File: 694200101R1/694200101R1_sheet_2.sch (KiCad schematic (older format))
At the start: 48 parts

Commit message: Added 3D Models
Added 3D Models for all components
Added Keyboard DXF for reference
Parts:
- D168, D169, D170, D171, D172, D173, D174, D175, D176, D177, D178, D179, D180, D181, D182, D183, D184, D185, D186, D187, D188, D189, D190, D191, D192, D193, D194, D195, D196, D197, D198, D199, D200, D201, D202, D203, D204, D205, D206, D207, D208, D209, D210, D211, D212, D213, D214, D215: renamed from D?; footprint LED_19-337C/RSBHGHC-A88/4T -> RSBHGHC-A88:4T; symbol 694200101-rescue:19-337C_RSBHGHC-A88_4T-19-337C_RSBHGHC-A88_4T -> 19-337C_RSBHGHC-A88_4T:RGB_LED

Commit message: fixed file names, added additional source
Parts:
- removed D168, D169, D170, D171, D172, D173, D174, D175, D176, D177, D178, D179, D180, D181, D182, D183, D184, D185, D186, D187, D188, D189, D190, D191, D192, D193, D194, D195, D196, D197, D198, D199, D200, D201, D202, D203, D204, D205, D206, D207, D208, D209, D210, D211, D212, D213, D214, D215: 19-337C_RSBHGHC-A88_4T, RSBHGHC-A88:4T, symbol 19-337C_RSBHGHC-A88_4T:RGB_LED
- added C10, C11, C13, C18, C20, C21, C23, C8: CL10B474KA8NFNC, capacitor-lib:CAPC1608X90N, symbol capacitor-lib:CL10B474KA8NFNC
- added C12, C14, C17, C19, C22, C9: CL10B104KB8NNNL, capacitor-lib:Samsung-CL10-09_2006-0-IPC_C, symbol capacitor-lib:CL10B104KB8NNNL
- added C15, C16: TAJB226K016RNJ, capacitor-lib:CAPPC3528X210N, symbol capacitor-lib:TAJB226K016RNJ
- added D104, D105, D106, D107, D108, D109, D110, D111, D112, D113, D114, D115, D116, D117, D118, D119, D120, D121, D122, D123, D124, D125, D126, D127, D128, D129, D130, D131, D132, D133, D134, D135, D136, D137, D138, D139, D140, D141, D142, D143, D144, D145, D146, D147, D148, D149, D150, D151, D152, D153, D154, D155, D156, D157, D158, D159, D160, D161, D162, D163, D164, D165, D166, D167: 19-337C_RSBHGHC-A88_4T, RSBHGHC-A88:4T, symbol 19-337C_RSBHGHC-A88_4T:RGB_LED
- added R10, R12, R13, R9: RMCF0603FT100K, Resistor-Libs:RESC1508X55N, symbol Resistor-Lib:RMCF0603FT100K
- added R11, R14: RMCF2512FT20K0, Resistor-Libs:RESC6332X70N, symbol Resistor-Lib:RMCF2512FT20K0
- added U3: M24M02-DRMN6TP, STM:STMicroelectronics-SO8N-SO-A-0-2-IPC_C, symbol STM:M24M02-DRMN6TP
- added U4, U5: IS31FL3733B-QFLS4-TR, Lumissil:IS31FL3733B-QFLS4-TR, symbol Lumissil:IS31FL3733B-QFLS4-TR
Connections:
- net CS10_B: now also U5.26 (CS10)
- net CS11_B: now also U5.27 (CS11)
- net CS12_B: now also U5.28 (CS12)
- net CS1_B: now also U5.16 (CS1)
- net CS2_B: now also U5.17 (CS2)
- net CS3_B: now also U5.18 (CS3)
- net CS4_B: now also U5.19 (CS4)
- net CS5_B: now also U5.21 (CS5)
- net CS6_B: now also U5.22 (CS6)
- net CS7_B: now also U5.23 (CS7)
- net CS8_B: now also U5.24 (CS8)
- net CS9_B: now also U5.25 (CS9)
- net SW10_B: now also U5.13 (SW10)
- net SW11_B: now also U5.14 (SW11)
- net SW12_B: now also U5.15 (SW12)
- net SW1_B: now also U5.2 (SW1)
- net SW2_B: now also U5.3 (SW2)
- net SW3_B: now also U5.4 (SW3)
- net SW4_B: now also U5.6 (SW4)
- net SW5_B: now also U5.7 (SW5)
- net SW6_B: now also U5.8 (SW6)
- net SW7_B: now also U5.9 (SW7)
- net SW8_B: now also U5.10 (SW8)
- net SW9_B: now also U5.11 (SW9)
- new net: R11.1, U4.35 (RSET)
- new net: R9.1, U4.47 (IICRST)
- new net: R14.1, U5.35 (RSET)
- new net: U5.42 (SCL), U5.43 (ADDR1)
- new net: R12.1, U5.47 (IICRST)
- new net +3V3: C10.1, C11.1, C12.1, C13.1, C14.1, C15.1, C16.1, C17.1, C18.1, C19.1, C20.1, C21.1, C22.1, C23.1, C8.1, C9.1, R10.1, R13.1, U3.8 (VCC), U4.20 (PVCC), U4.29 (PVCC), U4.37 (AVCC), U4.38 (DVCC), U4.39 (VIO), U4.46 (SDB), U5.20 (PVCC), U5.29 (PVCC), U5.37 (AVCC), U5.38 (DVCC), U5.39 (VIO), U5.46 (SDB)
- new net CS10_A: D140.2, D140.4, D140.6, D141.2, D141.4, D141.6, D142.2, D142.4, D142.6, D143.2, D143.4, D143.6, U4.26 (CS10)
- new net CS11_A: D144.2, D144.4, D144.6, D145.2, D145.4, D145.6, D146.2, D146.4, D146.6, D147.2, D147.4, D147.6, U4.27 (CS11)
- new net CS12_A: D148.2, D148.4, D148.6, D149.2, D149.4, D149.6, D150.2, D150.4, D150.6, D151.2, D151.4, D151.6, U4.28 (CS12)
- new net CS13_A: D152.2, D152.4, D152.6, D153.2, D153.4, D153.6, D154.2, D154.4, D154.6, D155.2, D155.4, D155.6, U4.30 (CS13)
- new net CS13_B: U5.30 (CS13)
- new net CS14_A: D156.2, D156.4, D156.6, D157.2, D157.4, D157.6, D158.2, D158.4, D158.6, D159.2, D159.4, D159.6, U4.31 (CS14)
- new net CS14_B: U5.31 (CS14)
- new net CS15_A: D160.2, D160.4, D160.6, D161.2, D161.4, D161.6, D162.2, D162.4, D162.6, D163.2, D163.4, D163.6, U4.32 (CS15)
- new net CS15_B: U5.32 (CS15)
- new net CS16_A: D164.2, D164.4, D164.6, D165.2, D165.4, D165.6, D166.2, D166.4, D166.6, D167.2, D167.4, D167.6, U4.33 (CS16)
- new net CS16_B: U5.33 (CS16)
- new net CS1_A: D104.2, D104.4, D104.6, D105.2, D105.4, D105.6, D106.2, D106.4, D106.6, D107.2, D107.4, D107.6, U4.16 (CS1)
- new net CS2_A: D108.2, D108.4, D108.6, D109.2, D109.4, D109.6, D110.2, D110.4, D110.6, D111.2, D111.4, D111.6, U4.17 (CS2)
- new net CS3_A: D112.2, D112.4, D112.6, D113.2, D113.4, D113.6, D114.2, D114.4, D114.6, D115.2, D115.4, D115.6, U4.18 (CS3)
- new net CS4_A: D116.2, D116.4, D116.6, D117.2, D117.4, D117.6, D118.2, D118.4, D118.6, D119.2, D119.4, D119.6, U4.19 (CS4)
- new net CS5_A: D120.2, D120.4, D120.6, D121.2, D121.4, D121.6, D122.2, D122.4, D122.6, D123.2, D123.4, D123.6, U4.21 (CS5)
- new net CS6_A: D124.2, D124.4, D124.6, D125.2, D125.4, D125.6, D126.2, D126.4, D126.6, D127.2, D127.4, D127.6, U4.22 (CS6)
- new net CS7_A: D128.2, D128.4, D128.6, D129.2, D129.4, D129.6, D130.2, D130.4, D130.6, D131.2, D131.4, D131.6, U4.23 (CS7)
- new net CS8_A: D132.2, D132.4, D132.6, D133.2, D133.4, D133.6, D134.2, D134.4, D134.6, D135.2, D135.4, D135.6, U4.24 (CS8)
- new net CS9_A: D136.2, D136.4, D136.6, D137.2, D137.4, D137.6, D138.2, D138.4, D138.6, D139.2, D139.4, D139.6, U4.25 (CS9)
- new net GND: C10.2, C11.2, C12.2, C13.2, C14.2, C15.2, C16.2, C17.2, C18.2, C19.2, C20.2, C21.2, C22.2, C23.2, C8.2, C9.2, R10.2, R11.2, R12.2, R13.2, R14.2, R9.2, U3.1 (DU), U3.2 (DU), U3.3 (E2), U3.4 (VSS), U3.7 (~WC~), U4.12 (PGND), U4.34 (AGND), U4.43 (ADDR1), U4.44 (ADDR2), U4.48 (GND), U4.49 (HTAB), U4.5 (PGND), U5.12 (PGND), U5.34 (AGND), U5.44 (ADDR2), U5.48 (GND), U5.49 (HTAB), U5.5 (PGND)
- new net SW10_A: D104.1, D108.1, D112.1, D116.1, D120.1, D124.1, D128.1, D132.1, D136.1, D140.1, D144.1, D148.1, D152.1, D156.1, D160.1, D164.1, U4.13 (SW10)
- new net SW11_A: D104.3, D108.3, D112.3, D116.3, D120.3, D124.3, D128.3, D132.3, D136.3, D140.3, D144.3, D148.3, D152.3, D156.3, D160.3, D164.3, U4.14 (SW11)
- new net SW12_A: D104.5, D108.5, D112.5, D116.5, D120.5, D124.5, D128.5, D132.5, D136.5, D140.5, D144.5, D148.5, D152.5, D156.5, D160.5, D164.5, U4.15 (SW12)
- new net SW1_A: D107.1, D111.1, D115.1, D119.1, D123.1, D127.1, D131.1, D135.1, D139.1, D143.1, D147.1, D151.1, D155.1, D159.1, D163.1, D167.1, U4.2 (SW1)
- new net SW2_A: D107.3, D111.3, D115.3, D119.3, D123.3, D127.3, D131.3, D135.3, D139.3, D143.3, D147.3, D151.3, D155.3, D159.3, D163.3, D167.3, U4.3 (SW2)
- new net SW3_A: D107.5, D111.5, D115.5, D119.5, D123.5, D127.5, D131.5, D135.5, D139.5, D143.5, D147.5, D151.5, D155.5, D159.5, D163.5, D167.5, U4.4 (SW3)
- new net SW4_A: D106.1, D110.1, D114.1, D118.1, D122.1, D126.1, D130.1, D134.1, D138.1, D142.1, D146.1, D150.1, D154.1, D158.1, D162.1, D166.1, U4.6 (SW4)
- new net SW5_A: D106.3, D110.3, D114.3, D118.3, D122.3, D126.3, D130.3, D134.3, D138.3, D142.3, D146.3, D150.3, D154.3, D158.3, D162.3, D166.3, U4.7 (SW5)
- new net SW6_A: D106.5, D110.5, D114.5, D118.5, D122.5, D126.5, D130.5, D134.5, D138.5, D142.5, D146.5, D150.5, D154.5, D158.5, D162.5, D166.5, U4.8 (SW6)
- new net SW7_A: D105.1, D109.1, D113.1, D117.1, D121.1, D125.1, D129.1, D133.1, D137.1, D141.1, D145.1, D149.1, D153.1, D157.1, D161.1, D165.1, U4.9 (SW7)
- new net SW8_A: D105.3, D109.3, D113.3, D117.3, D121.3, D125.3, D129.3, D133.3, D137.3, D141.3, D145.3, D149.3, D153.3, D157.3, D161.3, D165.3, U4.10 (SW8)
- new net SW9_A: D105.5, D109.5, D113.5, D117.5, D121.5, D125.5, D129.5, D133.5, D137.5, D141.5, D145.5, D149.5, D153.5, D157.5, D161.5, D165.5, U4.11 (SW9)
- new net SYNC: U4.40 (SYNC), U5.40 (SYNC)
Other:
- note added: "LED_DRIVER_A\nP20"
- note added: "LED_DRIVER_A\nP29"
- note added: "LED_DRIVER_A\nP37/38"
- note added: "LED_DRIVER_A\nP39"
- note added: "LED_DRIVER_A\nPWR_FILTER"
- note added: "LED_DRIVER_B\nP20"
- note added: "LED_DRIVER_B\nP29"
- note added: "LED_DRIVER_B\nP37/38"
- note added: "LED_DRIVER_B\nP39"
- note added: "LED_DRIVER_B\nPWR_FILTER"

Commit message: top row buttons
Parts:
- renumbered D104 to D109, D105 to D110, D106 to D111, D107 to D112, D108 to D113, D109 to D114, D110 to D115, D111 to D116, D112 to D117, D113 to D118, D114 to D119, D115 to D120, D116 to D121, D117 to D122, D118 to D123, D119 to D124, D120 to D125, D121 to D126, D122 to D127, D123 to D128, D124 to D129, D125 to D130, D126 to D131, D127 to D132, D128 to D133, D129 to D134, D130 to D135, D131 to D136, D132 to D137, D133 to D138, D134 to D139, D135 to D140, D136 to D141, D137 to D142, D138 to D143, D139 to D144, D140 to D145, D141 to D146, D142 to D147, D143 to D148, D144 to D149, D145 to D150, D146 to D151, D147 to D152, D148 to D153, D149 to D154, D150 to D155, D151 to D156, D152 to D157, D153 to D158, D154 to D159, D155 to D160, D156 to D161, D157 to D162, D158 to D163, D159 to D164, D160 to D165, D161 to D166, D162 to D167, D163 to D168, D164 to D169, D165 to D170, D166 to D171, D167 to D172

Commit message: diodes laidout
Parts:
- renumbered C8 to C11, C9 to C12, C10 to C13, C11 to C14, C12 to C15, C13 to C16, C14 to C17, C15 to C18, C16 to C19, C17 to C20, C18 to C21, C19 to C22, C20 to C23, C21 to C24, C22 to C25, C23 to C26, U3 to U4, U4 to U5, U5 to U6
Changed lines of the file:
@@
 Connection ~ 6550 1200
 $Comp
-L STM:M24M02-DRMN6TP U3
+L STM:M24M02-DRMN6TP U4
 U 1 1 63D31709
 P 1450 7600
-F 0 "U3" H 2050 7865 50  0000 C CNN
+F 0 "U4" H 2050 7865 50  0000 C CNN
 F 1 "M24M02-DRMN6TP" H 2050 7774 50  0000 L CNN
 F 2 "STM:STMicroelectronics-SO8N-SO-A-0-2-IPC_C" H 1450 8000 50  0001 L CNN
@@
 $EndComp
 $Comp
-L power:+3V3 #PWR012
+L power:+3V3 #PWR016
 U 1 1 63D43A95
 P 1500 7600
-F 0 "#PWR012" H 1500 7450 50  0001 C CNN
+F 0 "#PWR016" H 1500 7450 50  0001 C CNN
 F 1 "+3V3" H 1515 7773 50  0000 C CNN
 F 2 "" H 1500 7600 50  0001 C CNN
@@
 $EndComp
 $Comp
-L power:GND #PWR013
+L power:GND #PWR017
 U 1 1 63D489E9
 P 2550 8500
-F 0 "#PWR013" H 2550 8250 50  0001 C CNN
+F 0 "#PWR017" H 2550 8250 50  0001 C CNN
 F 1 "GND" H 2555 8327 50  0000 C CNN
 F 2 "" H 2550 8500 50  0001 C CNN
@@
 $EndComp
 $Comp
-L Lumissil:IS31FL3733B-QFLS4-TR U4
+L Lumissil:IS31FL3733B-QFLS4-TR U5
 U 1 1 63D4A2BB
 P 5800 7750
-F 0 "U4" H 6700 8137 60  0000 C CNN
+F 0 "U5" H 6700 8137 60  0000 C CNN
 F 1 "IS31FL3733B-QFLS4-TR" H 6700 8031 60  0000 C CNN
 F 2 "Lumissil:IS31FL3733B-QFLS4-TR" H 6700 7990 60  0001 C CNN
@@
 $EndComp
 $Comp
-L power:+3V3 #PWR024
+L power:+3V3 #PWR028
 U 1 1 63D70980
 P 13100 6800
-F 0 "#PWR024" H 13100 6650 50  0001 C CNN
+F 0 "#PWR028" H 13100 6650 50  0001 C CNN
 F 1 "+3V3" H 13115 6973 50  0000 C CNN
 F 2 "" H 13100 6800 50  0001 C CNN
@@
 $EndComp
 $Comp
-L capacitor-lib:CL10B474KA8NFNC C8
+L capacitor-lib:CL10B474KA8NFNC C11
 U 1 1 63D72369
 P 10100 7000
-F 0 "C8" V 10150 6850 50  0000 C CNN
+F 0 "C11" V 10150 6850 50  0000 C CNN
 F 1 "CL10B474KA8NFNC" V 10195 7103 50  0001 L BNN
 F 2 "capacitor-lib:CAPC1608X90N" H 10100 7000 50  0001 L BNN
@@
 $EndComp
 $Comp
-L capacitor-lib:CL10B104KB8NNNL C9
+L capacitor-lib:CL10B104KB8NNNL C12
 U 1 1 63D764B5
 P 10300 6950
-F 0 "C9" H 10473 6850 50  0000 C CNN
+F 0 "C12" H 10473 6850 50  0000 C CNN
 F 1 "CL10B104KB8NNNL" H 10428 6850 50  0001 L CNN
 F 2 "capacitor-lib:Samsung-CL10-09_2006-0-IPC_C" H 10300 7250 50  0001 L CNN
@@
 $EndComp
 $Comp
-L power:GND #PWR025
+L power:GND #PWR029
 U 1 1 63D793EB
 P 13100 7250
-F 0 "#PWR025" H 13100 7000 50  0001 C CNN
+F 0 "#PWR029" H 13100 7000 50  0001 C CNN
 F 1 "GND" H 13105 7077 50  0000 C CNN
 F 2 "" H 13100 7250 50  0001 C CNN
@@
 $EndComp
 $Comp
-L capacitor-lib:CL10B474KA8NFNC C10
+L capacitor-lib:CL10B474KA8NFNC C13
 U 1 1 63D81B26
 P 10900 7000
-F 0 "C10" V 11000 6850 50  0000 C CNN
+F 0 "C13" V 11000 6850 50  0000 C CNN
 F 1 "CL10B474KA8NFNC" V 10995 7103 50  0001 L BNN
 F 2 "capacitor-lib:CAPC1608X90N" H 10900 7000 50  0001 L BNN
@@
 $EndComp
 $Comp
-L power:+3V3 #PWR015
+L power:+3V3 #PWR019
 U 1 1 63D94BE2
 P 3600 8900
-F 0 "#PWR015" H 3600 8750 50  0001 C CNN
+F 0 "#PWR019" H 3600 8750 50  0001 C CNN
 F 1 "+3V3" H 3615 9073 50  0000 C CNN
 F 2 "" H 3600 8900 50  0001 C CNN
@@
 $EndComp
 $Comp
-L capacitor-lib:CL10B474KA8NFNC C11
+L capacitor-lib:CL10B474KA8NFNC C14
 U 1 1 63D9DE47
 P 11350 7000
-F 0 "C11" V 11450 6850 50  0000 C CNN
+F 0 "C14" V 11450 6850 50  0000 C CNN
 F 1 "CL10B474KA8NFNC" H 11350 6800 50  0001 L BNN
 F 2 "capacitor-lib:CAPC1608X90N" H 11350 7000 50  0001 L BNN
@@
 $EndComp
 $Comp
-L capacitor-lib:CL10B104KB8NNNL C12
+L capacitor-lib:CL10B104KB8NNNL C15
 U 1 1 63D9F36F
 P 11550 6950
-F 0 "C12" H 11723 6850 50  0000 C CNN
+F 0 "C15" H 11723 6850 50  0000 C CNN
 F 1 "CL10B104KB8NNNL" H 11550 7150 50  0001 L CNN
 F 2 "capacitor-lib:Samsung-CL10-09_2006-0-IPC_C" H 11550 7250 50  0001 L CNN
@@
 $EndComp
 $Comp
-L capacitor-lib:CL10B474KA8NFNC C13
+L capacitor-lib:CL10B474KA8NFNC C16
 U 1 1 63DE9808
 P 12150 7000
-F 0 "C13" V 12250 7150 50  0000 C CNN
+F 0 "C16" V 12250 7150 50  0000 C CNN
 F 1 "CL10B474KA8NFNC" H 12150 6800 50  0001 L BNN
 F 2 "capacitor-lib:CAPC1608X90N" H 12150 7000 50  0001 L BNN
@@
 $EndComp
 $Comp
-L power:GND #PWR014
+L power:GND #PWR018
 U 1 1 63EC1EB0
 P 3000 10150
-F 0 "#PWR014" H 3000 9900 50  0001 C CNN
+F 0 "#PWR018" H 3000 9900 50  0001 C CNN
 F 1 "GND" H 3005 9977 50  0000 C CNN
 F 2 "" H 3000 10150 50  0001 C CNN
@@
 $EndComp
 $Comp
-L power:GND #PWR016
+L power:GND #PWR020
 U 1 1 63EFD874
 P 3750 8250
-F 0 "#PWR016" H 3750 8000 50  0001 C CNN
+F 0 "#PWR020" H 3750 8000 50  0001 C CNN
 F 1 "GND" H 3755 8077 50  0000 C CNN
 F 2 "" H 3750 8250 50  0001 C CNN
@@
 $EndComp
 $Comp
-L Lumissil:IS31FL3733B-QFLS4-TR U5
+L Lumissil:IS31FL3733B-QFLS4-TR U6
 U 1 1 6409AB0A
 P 9900 7750
-F 0 "U5" H 10800 8137 60  0000 C CNN
+F 0 "U6" H 10800 8137 60  0000 C CNN
 F 1 "IS31FL3733B-QFLS4-TR" H 10800 8031 60  0000 C CNN
 F 2 "Lumissil:IS31FL3733B-QFLS4-TR" H 10800 7990 60  0001 C CNN
@@
 $EndComp
 $Comp
-L power:+3V3 #PWR020
+L power:+3V3 #PWR024
 U 1 1 6409AB1B
 P 7700 8900
-F 0 "#PWR020" H 7700 8750 50  0001 C CNN
+F 0 "#PWR024" H 7700 8750 50  0001 C CNN
 F 1 "+3V3" H 7715 9073 50  0000 C CNN
 F 2 "" H 7700 8900 50  0001 C CNN
@@
 $EndComp
 $Comp
-L power:GND #PWR019
+L power:GND #PWR023
 U 1 1 6409AB40
 P 7100 10150
-F 0 "#PWR019" H 7100 9900 50  0001 C CNN
+F 0 "#PWR023" H 7100 9900 50  0001 C CNN
 F 1 "GND" H 7105 9977 50  0000 C CNN
 F 2 "" H 7100 10150 50  0001 C CNN
@@
 $EndComp
 $Comp
-L power:GND #PWR021
+L power:GND #PWR025
 U 1 1 6409AB59
 P 7850 8250
-F 0 "#PWR021" H 7850 8000 50  0001 C CNN
+F 0 "#PWR025" H 7850 8000 50  0001 C CNN
 F 1 "GND" H 7855 8077 50  0000 C CNN
 F 2 "" H 7850 8250 50  0001 C CNN
@@
 $EndComp
 $Comp
-L power:+3V3 #PWR022
+L power:+3V3 #PWR026
 U 1 1 6409AB74
 P 10350 9600
-F 0 "#PWR022" H 10350 9450 50  0001 C CNN
+F 0 "#PWR026" H 10350 9450 50  0001 C CNN
 F 1 "+3V3" H 10365 9773 50  0000 C CNN
 F 2 "" H 10350 9600 50  0001 C CNN
@@
 $EndComp
 $Comp
-L power:GND #PWR023
+L power:GND #PWR027
 U 1 1 6409AB6A
 P 10400 8900
-F 0 "#PWR023" H 10400 8650 50  0001 C CNN
+F 0 "#PWR027" H 10400 8650 50  0001 C CNN
 F 1 "GND" H 10405 8727 50  0000 C CNN
 F 2 "" H 10400 8900 50  0001 C CNN
@@
 $EndComp
 $Comp
-L power:+3V3 #PWR017
+L power:+3V3 #PWR021
 U 1 1 63F20B48
 P 6250 9600
-F 0 "#PWR017" H 6250 9450 50  0001 C CNN
+F 0 "#PWR021" H 6250 9450 50  0001 C CNN
 F 1 "+3V3" H 6265 9773 50  0000 C CNN
 F 2 "" H 6250 9600 50  0001 C CNN
@@
 $EndComp
 $Comp
-L power:GND #PWR018
+L power:GND #PWR022
 U 1 1 63F0DD67
 P 6300 8900
-F 0 "#PWR018" H 6300 8650 50  0001 C CNN
+F 0 "#PWR022" H 6300 8650 50  0001 C CNN
 F 1 "GND" H 6305 8727 50  0000 C CNN
 F 2 "" H 6300 8900 50  0001 C CNN
@@
 	10100 6900 10300 6900
 $Comp
-L capacitor-lib:TAJB226K016RNJ C15
+L capacitor-lib:TAJB226K016RNJ C18
 U 1 1 63E8E5AC
 P 12800 7100
-F 0 "C15" V 12850 6950 50  0000 C TNN
+F 0 "C18" V 12850 6950 50  0000 C TNN
 F 1 "TAJB226K016RNJ" H 12800 6900 50  0001 L BNN
 F 2 "capacitor-lib:CAPPC3528X210N" H 12800 7100 50  0001 L BNN
@@
 $EndComp
 $Comp
-L capacitor-lib:CL10B104KB8NNNL C14
+L capacitor-lib:CL10B104KB8NNNL C17
 U 1 1 63DECC4B
 P 12350 6950
-F 0 "C14" H 12523 6850 50  0000 C CNN
+F 0 "C17" H 12523 6850 50  0000 C CNN
 F 1 "CL10B104KB8NNNL" H 12350 7150 50  0001 L CNN
 F 2 "capacitor-lib:Samsung-CL10-09_2006-0-IPC_C" H 12350 7250 50  0001 L CNN
@@
 	16100 6900 15900 6900
 $Comp
-L capacitor-lib:CL10B474KA8NFNC C18
+L capacitor-lib:CL10B474KA8NFNC C21
 U 1 1 63E29468
 P 14050 7050
-F 0 "C18" V 14100 7200 50  0000 C CNN
+F 0 "C21" V 14100 7200 50  0000 C CNN
 F 1 "CL10B474KA8NFNC" H 14050 6850 50  0001 L BNN
 F 2 "capacitor-lib:CAPC1608X90N" H 14050 7050 50  0001 L BNN
@@
 $EndComp
 $Comp
-L capacitor-lib:CL10B104KB8NNNL C17
+L capacitor-lib:CL10B104KB8NNNL C20
 U 1 1 63E29486
 P 13850 7000
-F 0 "C17" H 14023 6900 50  0000 C CNN
+F 0 "C20" H 14023 6900 50  0000 C CNN
 F 1 "CL10B104KB8NNNL" H 13850 7200 50  0001 L CNN
 F 2 "capacitor-lib:Samsung-CL10-09_2006-0-IPC_C" H 13850 7300 50  0001 L CNN
@@
 $EndComp
 $Comp
-L capacitor-lib:CL10B104KB8NNNL C19
+L capacitor-lib:CL10B104KB8NNNL C22
 U 1 1 63E29448
 P 14650 7000
-F 0 "C19" H 14823 6900 50  0000 C CNN
+F 0 "C22" H 14823 6900 50  0000 C CNN
 F 1 "CL10B104KB8NNNL" H 14650 7200 50  0001 L CNN
 F 2 "capacitor-lib:Samsung-CL10-09_2006-0-IPC_C" H 14650 7300 50  0001 L CNN
@@
 $EndComp
 $Comp
-L capacitor-lib:CL10B474KA8NFNC C20
+L capacitor-lib:CL10B474KA8NFNC C23
 U 1 1 63E2942E
 P 14850 7050
-F 0 "C20" V 14900 6900 50  0000 C CNN
+F 0 "C23" V 14900 6900 50  0000 C CNN
 F 1 "CL10B474KA8NFNC" H 14850 6850 50  0001 L BNN
 F 2 "capacitor-lib:CAPC1608X90N" H 14850 7050 50  0001 L BNN
@@
 $EndComp
 $Comp
-L capacitor-lib:CL10B474KA8NFNC C21
+L capacitor-lib:CL10B474KA8NFNC C24
 U 1 1 63E2941C
 P 15300 7050
-F 0 "C21" V 15350 6900 50  0000 C CNN
+F 0 "C24" V 15350 6900 50  0000 C CNN
 F 1 "CL10B474KA8NFNC" V 15395 7153 50  0001 L BNN
 F 2 "capacitor-lib:CAPC1608X90N" H 15300 7050 50  0001 L BNN
@@
 $EndComp
 $Comp
-L capacitor-lib:CL10B104KB8NNNL C22
+L capacitor-lib:CL10B104KB8NNNL C25
 U 1 1 63E2940D
 P 15900 7000
-F 0 "C22" H 16100 6900 50  0000 C CNN
+F 0 "C25" H 16100 6900 50  0000 C CNN
 F 1 "CL10B104KB8NNNL" H 16028 6900 50  0001 L CNN
 F 2 "capacitor-lib:Samsung-CL10-09_2006-0-IPC_C" H 15900 7300 50  0001 L CNN
@@
 	15900 7250 15900 7200
 $Comp
-L capacitor-lib:CL10B474KA8NFNC C23
+L capacitor-lib:CL10B474KA8NFNC C26
 U 1 1 63E293F3
 P 16100 7050
-F 0 "C23" V 16150 6900 50  0000 C CNN
+F 0 "C26" V 16150 6900 50  0000 C CNN
 F 1 "CL10B474KA8NFNC" V 16195 7153 50  0001 L BNN
 F 2 "capacitor-lib:CAPC1608X90N" H 16100 7050 50  0001 L BNN
@@
 $EndComp
 $Comp
-L capacitor-lib:TAJB226K016RNJ C16
+L capacitor-lib:TAJB226K016RNJ C19
 U 1 1 63E9B64D
 P 13400 7100
-F 0 "C16" V 13450 6952 50  0000 C CNN
+F 0 "C19" V 13450 6952 50  0000 C CNN
 F 1 "TAJB226K016RNJ" H 13400 6900 50  0001 L BNN
 F 2 "capacitor-lib:CAPPC3528X210N" H 13400 7100 50  0001 L BNN

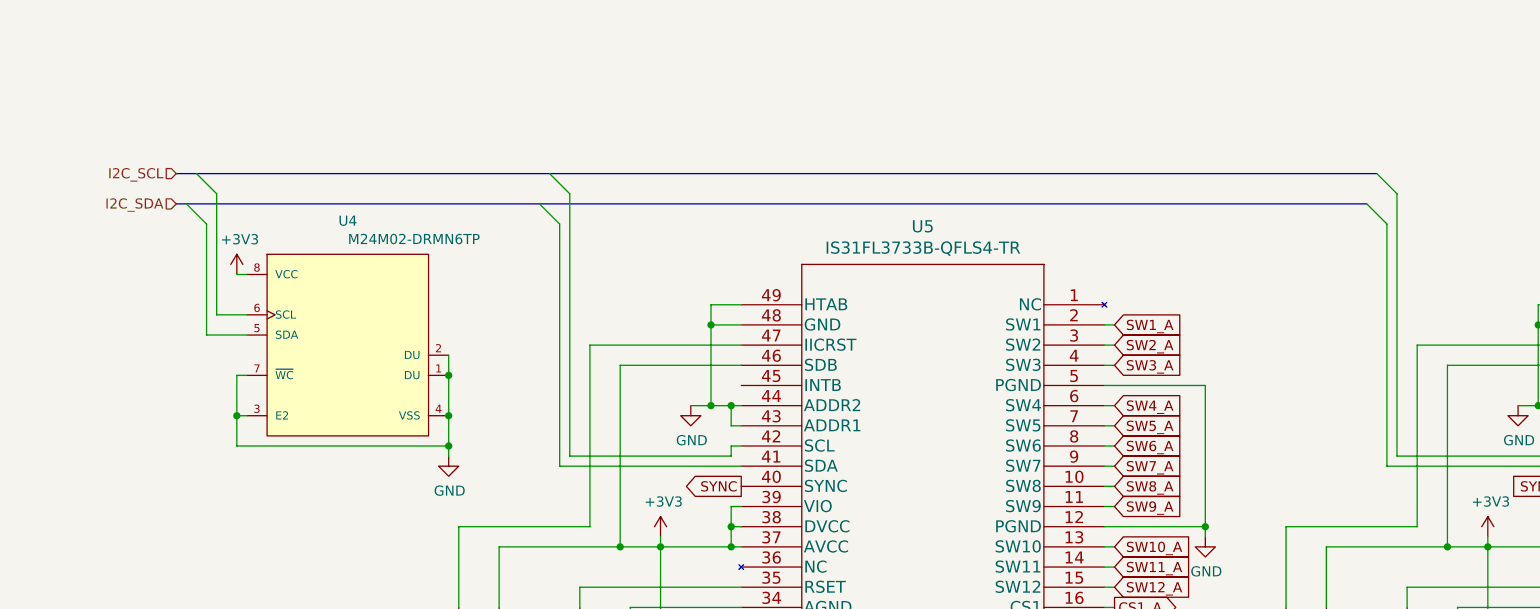
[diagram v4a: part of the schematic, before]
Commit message: Fixed Missing I2C Net
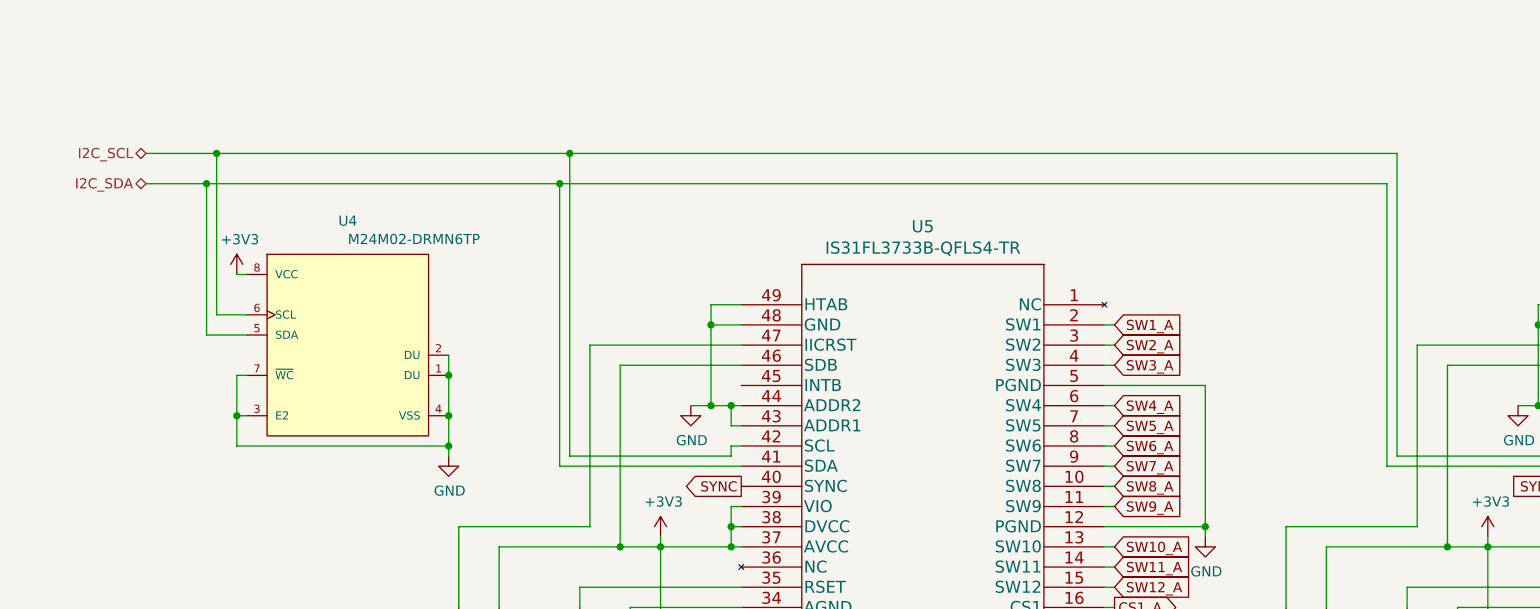
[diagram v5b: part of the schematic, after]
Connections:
- net I2C_SCL: now also U4.6 (SCL), U5.42 (SCL), U6.42 (SCL), U6.43 (ADDR1)
- net I2C_SDA: now also U4.5 (SDA), U5.41 (SDA), U6.41 (SDA)
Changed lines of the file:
@@
 Comment4 ""
 $EndDescr
-Text HLabel 1200 7250 0    50   Input ~ 0
+Text HLabel 1050 7150 0    50   BiDi ~ 0
 I2C_SDA
-Text HLabel 1200 7100 0    50   Input ~ 0
+Text HLabel 1050 7000 0    50   BiDi ~ 0
 I2C_SCL
-Entry Wire Line
-	1250 7250 1350 7350
-Entry Wire Line
-	1300 7100 1400 7200
 Wire Wire Line
 	1550 7900 1350 7900
 Wire Wire Line
-	1350 7900 1350 7350
-Wire Wire Line
-	1400 7200 1400 7800
-Wire Wire Line
 	1400 7800 1550 7800
 Wire Wire Line
@@
 Connection ~ 2550 8300
 Connection ~ 2550 8450
-Entry Wire Line
-	3000 7250 3100 7350
-Wire Wire Line
-	3100 7350 3100 8550
 Wire Wire Line
 	3100 8550 4000 8550
-Entry Wire Line
-	3050 7100 3150 7200
 Wire Wire Line
 	10300 6900 10300 6950
@@
 	3950 8500 3150 8500
 Wire Wire Line
-	3150 7200 3150 8500
-Wire Wire Line
 	5800 9650 6250 9650
 Wire Wire Line
@@
 Wire Wire Line
 	4000 9350 3950 9350
-Entry Wire Line
-	7100 7250 7200 7350
-Entry Wire Line
-	7150 7100 7250 7200
-Wire Wire Line
-	7200 7350 7200 8550
 Wire Wire Line
 	7200 8550 8100 8550
@@
 	8050 8500 7250 8500
 Wire Wire Line
-	7250 7200 7250 8500
-Wire Wire Line
 	9900 8850 10400 8850
 Wire Wire Line
@@
 Wire Wire Line
 	13100 7250 13400 7250
-Wire Bus Line
-	1200 7250 7100 7250
-Wire Bus Line
-	1200 7100 7150 7100
+Wire Wire Line
+	7200 7150 7200 8550
+Wire Wire Line
+	1050 7150 1350 7150
+Wire Wire Line
+	1350 7150 1350 7900
+Connection ~ 1350 7150
+Wire Wire Line
+	1350 7150 3100 7150
+Wire Wire Line
+	3100 7150 3100 8550
+Connection ~ 3100 7150
+Wire Wire Line
+	3100 7150 7200 7150
+Wire Wire Line
+	7250 7000 7250 8500
+Wire Wire Line
+	1050 7000 1400 7000
+Wire Wire Line
+	1400 7000 1400 7800
+Connection ~ 1400 7000
+Wire Wire Line
+	3150 7000 3150 8500
+Wire Wire Line
+	1400 7000 3150 7000
+Connection ~ 3150 7000
+Wire Wire Line
+	3150 7000 7250 7000
 $EndSCHEMATC
